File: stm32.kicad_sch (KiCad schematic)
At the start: 27 parts, among them J13 Screw_Terminal_01x04, U22 REF3030, U24 STM32F407VGTx, Y4 8Mhz

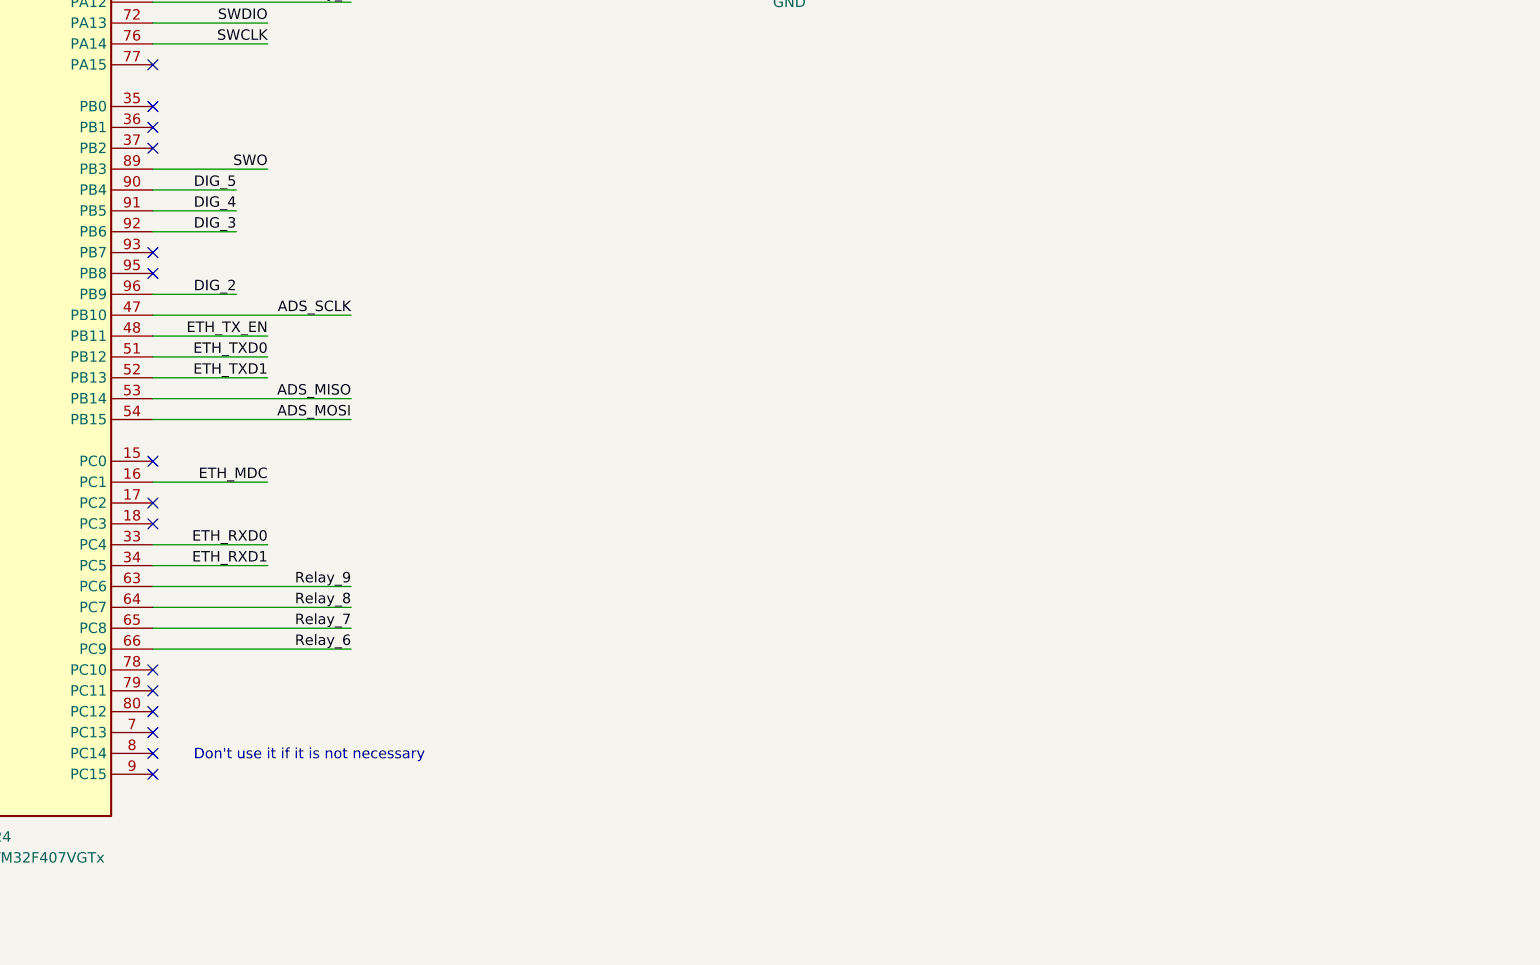
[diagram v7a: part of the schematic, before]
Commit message: Se añade led de status y eeprom externa. Se actualiza pcb y se añade serigrafía adicional. Se actualiza los componentes jlcpcb, se utiliza un micro con con 512kbytes de flash a recomendacion de jefry debido a la escasez de los de 1024 kbytes. Se revisa y se espera mandar a china
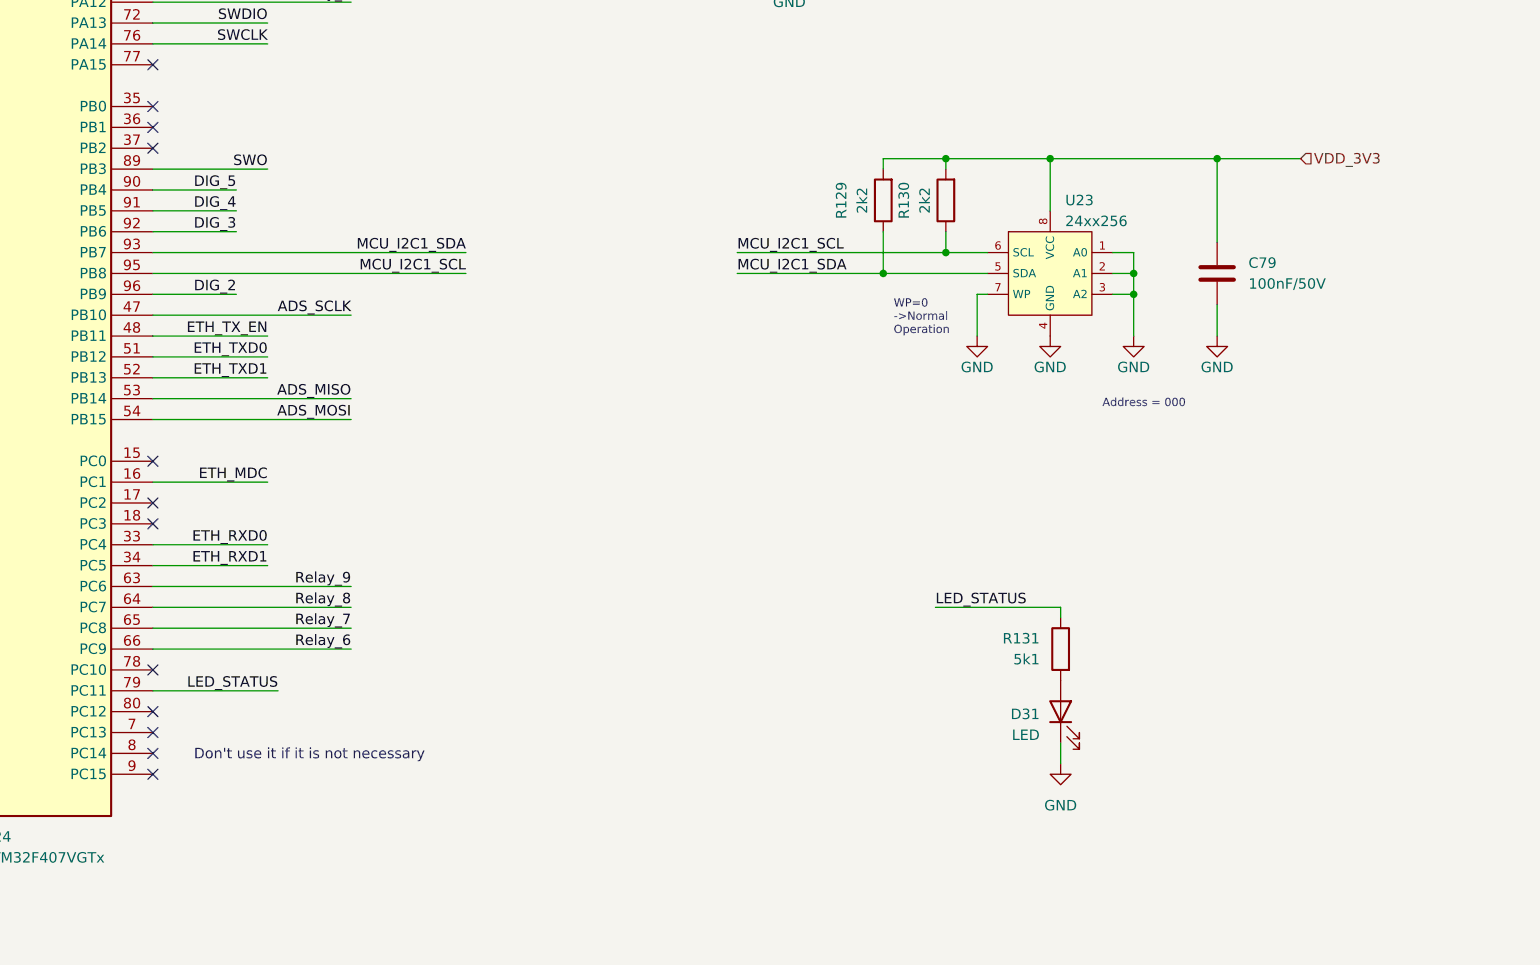
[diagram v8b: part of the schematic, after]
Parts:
- added C79: 100nF/50V, 1-Capacitor:C_0603_1608Metric, symbol 1-Capacitor:C_0603
- added D31: LED, LED_SMD:LED_0805_2012Metric, symbol Device:LED
- added R129, R130: 2k2, Resistor_SMD:R_0603_1608Metric, symbol 1-Resistor:R_0603
- added R131: 5k1, Resistor_SMD:R_0603_1608Metric, symbol Device:R
- added U23: 24xx256, Package_SO:SO-8_3.9x4.9mm_P1.27mm, symbol 1-IC-General:24xx256
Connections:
- net GND: now also C79.2, D31.1 (K), U23.1 (A0), U23.2 (A1), U23.3 (A2), U23.4 (GND), U23.7 (WP)
- net VDD_3V3: now also C79.1, R129.2, R130.2, U23.8 (VCC)
- net LED_STATUS: now reaches U24.79 (PC11)
- net LED_STATUS: now also R131.1
- net MCU_I2C1_SDA: now reaches U24.93 (PB7)
- net MCU_I2C1_SDA: now also R129.1, U23.5 (SDA)
- net MCU_I2C1_SCL: now reaches U24.95 (PB8)
- net MCU_I2C1_SCL: now also R130.1, U23.6 (SCL)
- new net: D31.2 (A), R131.2
- no-connect marks 40 -> 37
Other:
- note added: "Address = 000"
- note added: "WP=0 ->Normal Operation"
